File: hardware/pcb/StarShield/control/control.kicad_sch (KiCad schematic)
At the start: 9 parts, among them J3A nice!nano v2 左列 (PM 1-12), J3B nice!nano v2 右列 (PM 13-24), SW1 PCM13 (SP3T), U2 74HC595, U3 74HC595, U4 74HC595

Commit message: feat(schematic): M5 RGB 子图 —— 95 颗 SK6812MINI-E 数据链，原理图四张子图齐
新增第 6 张子图 rgb/rgb.kicad_sch（A2；95 灯珠 / 380 条引脚连接）：
- 数据源 rgb_design.py 由 docs/_generated/matrix.json 循环生成（位号 LED1..95 ↔ 键 index），
  链序 = 键位 index 顺序（行优先、行内从左到右），与 ZMK 侧 LED index 一致。
- LED1.DIN ← 全局 LED_DIN（控制子图 J3A.1 = P0.06 / spi3 MOSI）；LED95.DOUT 链尾 NC。
- 供电：全部 VDD → 全局 VLED（电源子图 Q1 门控的电池直供轨）；VSS → GND。
- 符号用官方 LED:SK6812MINI-E（派生符号已展平）；封装选 PLCC4 3.5x3.5 正装，
  型号-封装对应与贴装方向标 UNVERIFIED（B3/B4 用实物核对）。
- 根图改 3 列 x 2 行布局以容纳 6 张子图。
- verify_rgb.py：派生 / 跨图接口 / 具名（链序、链尾、供电）/ ERC 四组断言。

ERC：根图整体 0 error，isolated 两条（VLED / LED_DIN）就此归零。
同步：控制子图与 RGB 子图移除重复的 GND PWR_FLAG（全局网只能有一个 power output，
否则触发 ERC pin_to_pin error），改由电源子图统一提供；verify_control 断言同步。
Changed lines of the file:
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@@
-		(pin "1")
-	)
-	(symbol (lib_id "power:PWR_FLAG") (at 33.02 171.45 0) (unit 1)
-		(exclude_from_sim no) (in_bom yes) (on_board yes) (dnp no) (fields_autoplaced yes)
-	(property "Reference" "#FLG01" (at 33.02 166.37 0)
-			(effects (font (size 1.27 1.27)) (hide yes)))
-	(property "Value" "PWR_FLAG" (at 33.02 176.53 0)
-			(effects (font (size 1.27 1.27)) (hide yes)))
-	(property "Footprint" "" (at 33.02 171.45 0)
-			(effects (font (size 1.27 1.27)) (hide yes)))
-	(property "Datasheet" "" (at 33.02 171.45 0)
-			(effects (font (size 1.27 1.27)) (hide yes)))
-		(pin "1")
-	)
-	(symbol (lib_id "power:GND") (at 33.02 171.45 0) (unit 1)
-		(exclude_from_sim no) (in_bom yes) (on_board yes) (dnp no) (fields_autoplaced yes)
-	(property "Reference" "#PWR02175" (at 33.02 166.37 0)
-			(effects (font (size 1.27 1.27)) (hide yes)))
-	(property "Value" "GND" (at 33.02 176.53 0)
-			(effects (font (size 1.27 1.27)) (hide yes)))
-	(property "Footprint" "" (at 33.02 171.45 0)
-			(effects (font (size 1.27 1.27)) (hide yes)))
-	(property "Datasheet" "" (at 33.02 171.45 0)
-			(effects (font (size 1.27 1.27)) (hide yes)))
 		(pin "1")
 	)

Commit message: feat(b3): 新增封装存在性核查 + 排针封装定案
- 新增 docs/_tools/verify_footprints.py：扫描 4 张子图的 Footprint 属性，
  逐个去 KiCad 封装库查存在性 —— 「封装存不存在」从此是可复现断言，
  不再靠人工看（95 个热插拔座封装缺失就是这样默默存在的）。
- 实测：218 / 313 个元件的封装在官方库（13 种）。
- J3A/J3B 定案 Connector_PinSocket_2.54mm:PinSocket_1x12_P2.54mm_Vertical
  （官方库无 Connector_Mill-Max；排母孔径 1.0 vs Mill-Max 推荐 0.94mm 可焊，
  料号与孔径并入 B6 实物核对）。
- 唯一未决：MX 热插拔座封装（95 个）—— 官方库没有；社区库 CC BY-SA 4.0
  无官方库的「用于设计不受约束」例外，抄了会污染 CERN-OHL-S 链 ⇒ 不可引入。
  出路为「自画」或「改轴体直焊（官方封装现成且键宽全覆盖）」，待用户拍板。
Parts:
- J3A, J3B: footprint ❓待定（Mill-Max 插座，B3/B4 定） -> Connector_PinSocket_2.54mm:PinSocket_1x12_P2.54mm_Vertical; MPN (none) -> Mill-Max 315-43-112-41-001000 ❓待核
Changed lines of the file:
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@@
 	(property "Value" "nice!nano v2 左列 (PM 1-12)" (at 50.8 144.78 0)
 			(effects (font (size 1.27 1.27))))
-	(property "Footprint" "❓待定（Mill-Max 插座，B3/B4 定）" (at 50.8 139.7 0)
+	(property "Footprint" "Connector_PinSocket_2.54mm:PinSocket_1x12_P2.54mm_Vertical" (at 50.8 139.7 0)
 			(effects (font (size 1.27 1.27)) (hide yes)))
 	(property "Datasheet" "" (at 50.8 139.7 0)
+			(effects (font (size 1.27 1.27)) (hide yes)))
+		(property "MPN" "Mill-Max 315-43-112-41-001000 ❓待核" (at 50.8 139.7 0)
 			(effects (font (size 1.27 1.27)) (hide yes)))
 		(property "Note" "J3A.n = Pro Micro 标号 n；映射依据 ZMK arduino_pro_micro_pins.dtsi" (at 50.8 139.7 0)
@@
 	(property "Value" "nice!nano v2 右列 (PM 13-24)" (at 76.2 144.78 0)
 			(effects (font (size 1.27 1.27))))
-	(property "Footprint" "❓待定（Mill-Max 插座，B3/B4 定）" (at 76.2 139.7 0)
+	(property "Footprint" "Connector_PinSocket_2.54mm:PinSocket_1x12_P2.54mm_Vertical" (at 76.2 139.7 0)
 			(effects (font (size 1.27 1.27)) (hide yes)))
 	(property "Datasheet" "" (at 76.2 139.7 0)
 			(effects (font (size 1.27 1.27)) (hide yes)))
+		(property "MPN" "Mill-Max 315-43-112-41-001000 ❓待核" (at 76.2 139.7 0)
+			(effects (font (size 1.27 1.27)) (hide yes)))
 		(property "Note" "J3B.n = Pro Micro 标号 12+n；RAW(PM13) 接 OUT，VCC(PM16) 是 3.3V 轨" (at 76.2 139.7 0)

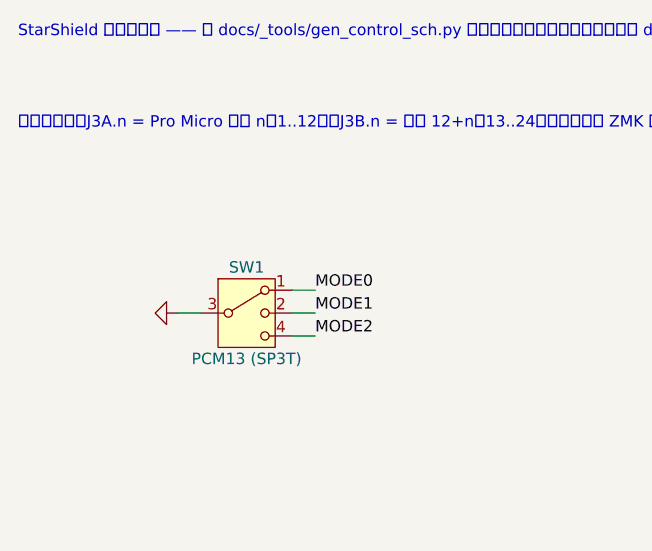
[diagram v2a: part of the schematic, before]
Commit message: fix(hw): 三档开关位号 SW1 -> SW96（与矩阵第一个开关重名）
根图整体网表里两个元件的引脚会并到同一个位号下；PCB 上会出现两个 SW1。
现有校验假通过：verify_netlist 数的是 SW 前缀的不同名字个数，
95 个矩阵开关 + 1 个 SP3T 因重名去重后仍是 95 个。

- control_design.py: ref 与 4 条连接改名 SW96（顺延 D96 的编号习惯）
- verify_control.py: 4 条开关断言改按 SW96
- verify_netlist.py: 矩阵开关显式只数 SW1..SW95（不再用前缀计数）
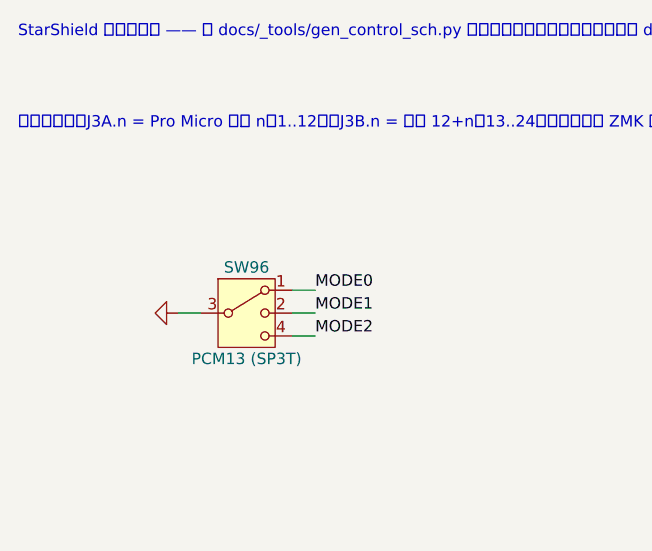
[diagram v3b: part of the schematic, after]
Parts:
- removed SW1: PCM13 (SP3T), Button_Switch_SMD:SW_SP3T_PCM13, symbol Switch:SW_SP3T
- added SW96: PCM13 (SP3T), Button_Switch_SMD:SW_SP3T_PCM13, symbol Switch:SW_SP3T
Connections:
- net GND: now also SW96.3
- net MODE0: now also SW96.1
- net MODE1: now also SW96.2
- net MODE2: now also SW96.4
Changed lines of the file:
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@@
 	(symbol (lib_id "Switch:SW_SP3T") (at 50.8 63.5 0) (unit 1)
 		(exclude_from_sim no) (in_bom yes) (on_board yes) (dnp no) (fields_autoplaced yes)
-	(property "Reference" "SW1" (at 50.8 58.42 0)
+	(property "Reference" "SW96" (at 50.8 58.42 0)
 			(effects (font (size 1.27 1.27))))
 	(property "Value" "PCM13 (SP3T)" (at 50.8 68.58 0)

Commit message: fix(b6-1): J3A/J3B 由 1x12 改 1x13（按 nice!nano v2 实物孔序），走线零改动
背景：2026-09-19 实物核对发现 nice!nano v2 每排 13 孔（官方 pinout 图 + 实物清点），
原 1x12 设计会把 J3B 的 VCC 插到实物 RESET 上、J3A 整排错位一孔。

关键洞察：官方孔序去掉第 1 孔后与旧 12 孔的网**逐孔一致** ⇒
只需在 USB 端左侧（x=37.46）加一个孔（J3A 加 GND、J3B 加 OUT）+ Pad 号整体后移一位，
**走线一根都不用动**。（反面做法「网络整体后移一孔」实测撞出 8 处 shorting_items +
2 处 tracks_crossing，已否决。）

改动：
- extract_power_symbols.py：符号缓存加 Connector_Generic:Conn_01x13（取代 01x12）
- control_design.py：J3A/J3B 改 Conn_01x13、CONN 表按官方孔序重排、页脚注更新
- control.kicad_sch / rgb.kicad_sch：生成链重跑产物
- verify_control.py / verify_rgb.py：断言孔号同步（LED_DIN 由 J3A.1 改 J3A.2）
- rgb_design.py：注释里的 J3A.1 改 J3A 孔2
- Starshield.kicad_pcb：J3A/J3B 各加第 13 孔、Pad 号重排、J3B 孔1-孔2 OUT 同网桥、
  重填铺铜（未连通 0、未豁免 error 0）
- docs/nice-nano-physical-verification.md：§4 落点修正（座口 x≈32.2）、§6 量测结论与执行记录

校验：七项校验器全绿；生成链确定性复核通过（重跑生成器后 git status 无变化）。
固件 overlay 零改动（D 编号 ↔ GPIO 映射不变）。
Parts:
- J3A: value nice!nano v2 左列 (PM 1-12) -> nice!nano v2 左列 (孔 1-13); footprint Connector_PinSocket_2.54mm:PinSocket_1x12_P2.54mm_Vertical -> Connector_PinSocket_2.54mm:PinSocket_1x13_P2.54mm_Vertical; symbol Connector_Generic:Conn_01x12 -> Connector_Generic:Conn_01x13; MPN Mill-Max 315-43-112-41-001000 ❓待核 -> Mill-Max 315-43-113-41-001000 ❓待核; Note J3A.n = Pro Micro 标号 n；映射依据 ZMK arduino_pro_micro_pins.dtsi -> J3A.n = 实物孔位序号（USB 端起）；D 编号见注释，依据 ZMK gpio-map
- J3B: value nice!nano v2 右列 (PM 13-24) -> nice!nano v2 右列 (孔 1-13); footprint Connector_PinSocket_2.54mm:PinSocket_1x12_P2.54mm_Vertical -> Connector_PinSocket_2.54mm:PinSocket_1x13_P2.54mm_Vertical; symbol Connector_Generic:Conn_01x12 -> Connector_Generic:Conn_01x13; MPN Mill-Max 315-43-112-41-001000 ❓待核 -> Mill-Max 315-43-113-41-001000 ❓待核; Note J3B.n = Pro Micro 标号 12+n；RAW(PM13) 接 OUT，VCC(PM16) 是 3.3V 轨 -> J3B.1/2 = B+(RAW) 接 OUT；孔 5 = 3.3V(VCC)；孔 4 = RESET 不接
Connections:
- net 595_MOSI: now also J3B.12 (Pin_12); no longer J3B.11 (Pin_11)
- net 595_RCLK: now also J3B.8 (Pin_8); no longer J3B.7 (Pin_7)
- net 595_SCK: now also J3B.10 (Pin_10); no longer J3B.9 (Pin_9)
- net GND: now also J3A.1 (Pin_1), J3A.5 (Pin_5), J3B.3 (Pin_3); no longer J3A.3 (Pin_3), J3B.2 (Pin_2)
- net LED_DIN: now also J3A.2 (Pin_2); no longer J3A.1 (Pin_1)
- net MODE0: now also J3A.6 (Pin_6); no longer J3A.5 (Pin_5)
- net MODE1: now also J3B.11 (Pin_11); no longer J3B.10 (Pin_10)
- net MODE2: now also J3B.9 (Pin_9); no longer J3B.8 (Pin_8)
- net OUT: now also J3B.2 (Pin_2)
- net RGB_PWR_EN: now also J3B.13 (Pin_13); no longer J3B.12 (Pin_12)
- net ROW0: now also J3A.8 (Pin_8); no longer J3A.7 (Pin_7)
- net ROW1: now also J3A.9 (Pin_9); no longer J3A.8 (Pin_8)
- net ROW2: now also J3A.10 (Pin_10); no longer J3A.9 (Pin_9)
- net ROW3: now also J3A.11 (Pin_11); no longer J3A.10 (Pin_10)
- net ROW4: now also J3A.13 (Pin_13); no longer J3A.12 (Pin_12)
- net ROW5: now also J3A.12 (Pin_12); no longer J3A.11 (Pin_11)
- net VCC: now also J3B.5 (Pin_5); no longer J3B.4 (Pin_4)
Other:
- note added: "【供电】J3B.1/2(B+) 接电源子图 OUT（系统轨 3.0-4.4V，电池/USB 较高者）—— nice!nano 板载稳压后输出 VCC(孔 5) 3.3V，给 3 颗 595 供电（负载轻，远低于 VCC 能力）。WS2812 供电走 VLED（电源子图 Q1 门控后的 LED 轨），不在本子图 —— 见 RGB 子图(M5)"
- note added: "【投板前核对】1) nice!nano 排针 pitch/脚数已由 B6 实物核对（每排 13 孔，已改 1x13）2) PCM13 封装 pad 与符号掷点对应（B3/B4）3) J3A.12/13 = ROW5/ROW4 的交错顺序与 overlay row-gpios 一一对应（已按 overlay 核实，但 PCB 布局时仍需复核）4) 排针针径与母座孔径、第五项：USB 口伸出量决定外壳开孔"
- note added: "【排针映射】J3A.n / J3B.n = nice!nano v2 **实物孔位序号（自 USB 端起，每排 13 孔）**。2026-09-19 B6 实物核对 + 官方 pinout 图确认每排 13 孔（比 Pro Micro 多 1 孔，多在 USB 端）；原 1x12 映射已作废。D 编号 ↔ GPIO 仍依 ZMK arduino_pro_micro_pins.dtsi，与孔位序号无关。逐孔映射表见 docs/nice-nano-physical-verification.md §6.2"
- note removed: "【供电】J3B.13(RAW) 接电源子图 OUT（系统轨 3.0-4.4V，电池/USB 较高者）—— nice!nano 板载稳压后输出 VCC(PM16) 3.3V，给 3 颗 595 供电（负载轻，远低于 VCC 能力）。WS2812 供电走 VLED（电源子图 Q1 门控后的 LED 轨），不在本子图 —— 见 RGB 子图(M5)"
- note removed: "【投板前核对】1) nice!nano 排针 pitch/脚数（B6）2) PCM13 封装 pad 与符号掷点对应（B3/B4）3) J3A.11/12 = ROW5/ROW4 的交错顺序与 overlay row-gpios 一一对应（已按 overlay 核实，但 PCB 布局时仍需复核）"
- note removed: "【排针映射】J3A.n = Pro Micro 标号 n（1..12），J3B.n = 标号 12+n（13..24）。映射来自 ZMK 官方 v0.3 nice_nano 的 arduino_pro_micro_pins.dtsi。投板前必须用实物核对排针 pitch / 每边脚数（handoff B6）"

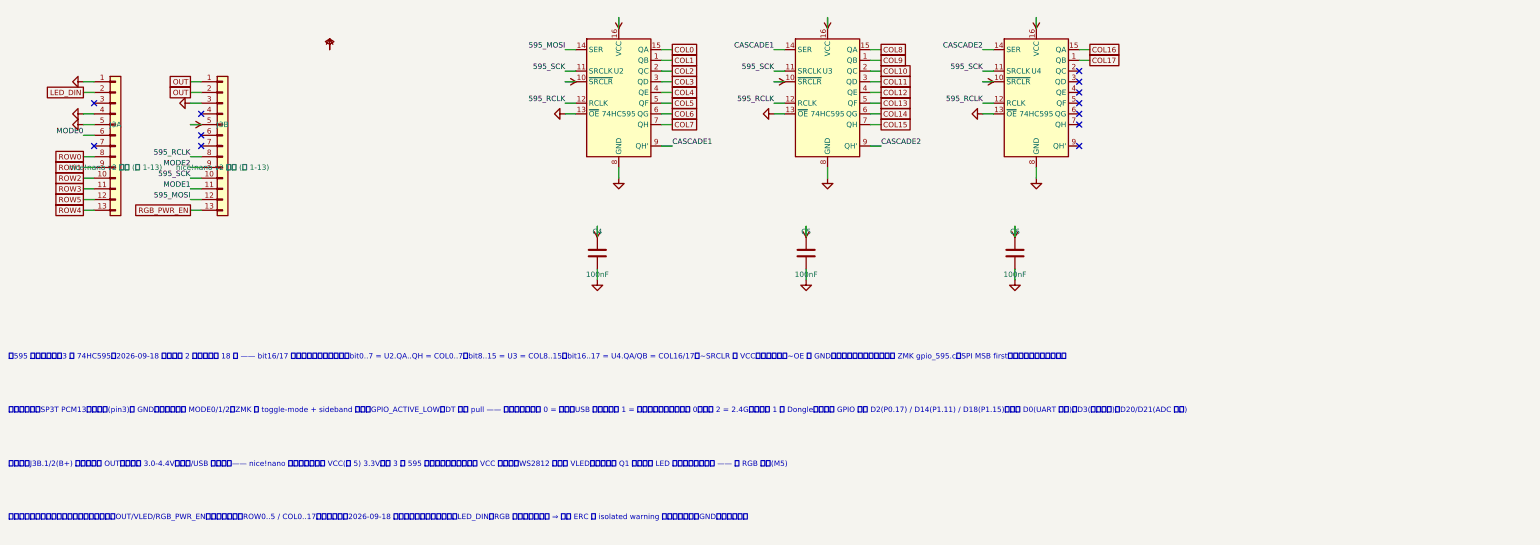
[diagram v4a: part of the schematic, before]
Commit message: feat(power): 方案①落地 —— 模块 B+/RAW 由 OUT 改接 VBAT（插模块口即充电）；模块整组左移 + J1 让位
背景（用户质疑成立）：商业键盘一律「一个口 = 数据 + 充电」（Kisnt KN85 / 雷柏 V700-8A /
CHERRY KW 9200 官方口径）；社区 nice!nano 方案把电池挂在模块自带充电器输出上，插模块口即充电。
我们原先把电池接自研 BQ24072 的 BAT、模块挂 OUT ⇒ 模块充电器的电流进不了电池
（OUT→BAT 不是充电路径）⇒ 有线模式下充不上电。

改动：
- 电路：J3B 孔1/孔2（B+/RAW）网络 OUT -> VBAT；VBAT 由电源子图局部网升为跨子图全局网
  （power_design.py 与 control_design.py 的 GLOBAL_NETS 各加 VBAT）
- 子图：power.kicad_sch / control.kicad_sch 重生成（版式自检通过）
- 校验：verify_control 断言改为「VBAT 跨图连通（J3B 孔1/2 + U1/J2/C3）」+
  「OUT 不再挂 J3B」；网表类五项校验全绿
- 几何（B6-2）：nice!nano 插座整组左移 30.46 mm（孔1 x=7.00、口面 x=1.70 与壳面齐平）；
  J1/R1/R2/F1 让位到 x=155-168；pcb_design.py 同步
- 板文件：J3B 孔1/2 改网为 VBAT（旧 OUT 走线已随左移一并清除）
- 文档：power-architecture.md §1 / bq24072-pinout.md §2.3 / decisions.md 电源段各加「重载仍接 OUT、
  模块为唯一例外」的修订说明；量测文档 §6.6 记录完整对标与代价

⚠️ 遗留（下一步）：肩部走线缺口待补（左移时删了 76 项），Freerouting 正在用新网表全板重布；
完成后需重跑 DRC + 七项校验器。
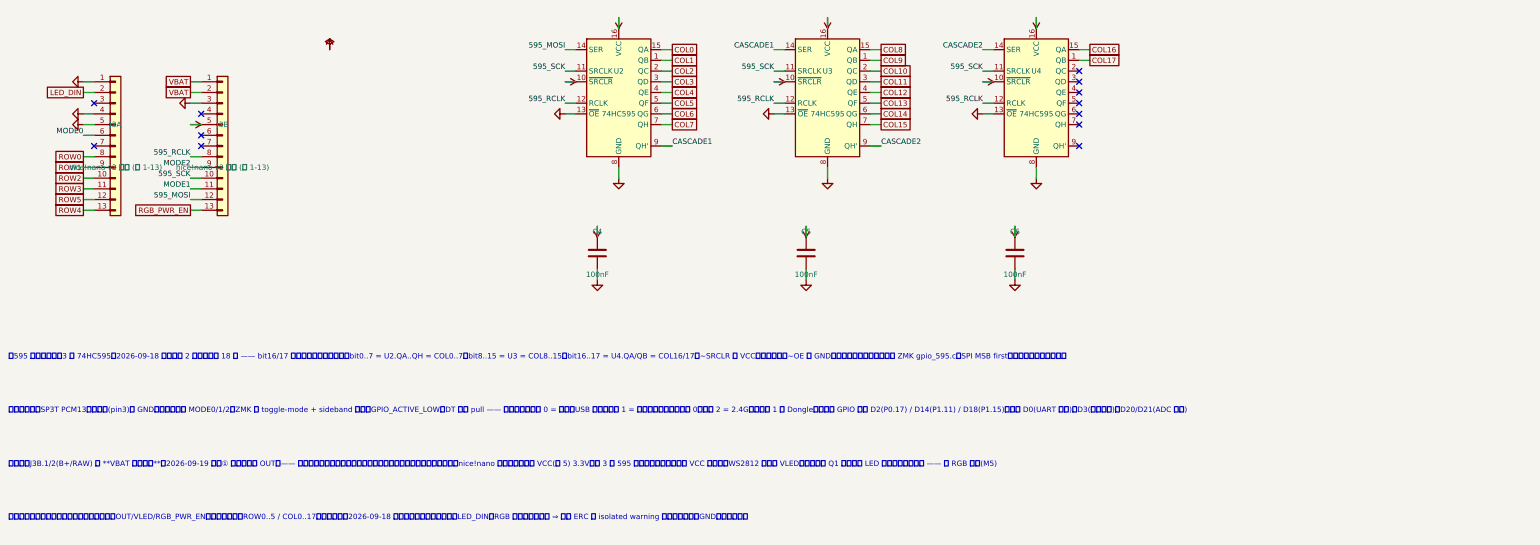
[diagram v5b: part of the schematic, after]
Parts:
- J3B: Note J3B.1/2 = B+(RAW) 接 OUT；孔 5 = 3.3V(VCC)；孔 4 = RESET 不接 -> J3B.1/2 = B+/RAW 接 VBAT 电池节点（2026-09-19 方案①）；孔 5 = 3.3V(VCC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
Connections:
- net OUT renamed VBAT
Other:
- note added: "【供电】J3B.1/2(B+/RAW) 接 **VBAT 电池节点**（2026-09-19 方案① 改接，原为 OUT）—— 如此插模块口即由模块自带充电器给电池充电（有线模式也充电）。nice!nano 板载稳压后输出 VCC(孔 5) 3.3V，给 3 颗 595 供电（负载轻，远低于 VCC 能力）。WS2812 供电走 VLED（电源子图 Q1 门控后的 LED 轨），不在本子图 —— 见 RGB 子图(M5)"
- note removed: "【供电】J3B.1/2(B+) 接电源子图 OUT（系统轨 3.0-4.4V，电池/USB 较高者）—— nice!nano 板载稳压后输出 VCC(孔 5) 3.3V，给 3 颗 595 供电（负载轻，远低于 VCC 能力）。WS2812 供电走 VLED（电源子图 Q1 门控后的 LED 轨），不在本子图 —— 见 RGB 子图(M5)"
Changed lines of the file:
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@@
 	(wire (pts (xy 71.12 124.46) (xy 68.58 124.46))
 		(stroke (width 0) (type default)))
-	(global_label "OUT" (shape passive) (at 68.58 124.46 180) (fields_autoplaced yes)
+	(global_label "VBAT" (shape passive) (at 68.58 124.46 180) (fields_autoplaced yes)
 		(effects (font (size 1.27 1.27)) (justify right))
 	)
 	(wire (pts (xy 71.12 127.0) (xy 68.58 127.0))
 		(stroke (width 0) (type default)))
-	(global_label "OUT" (shape passive) (at 68.58 127.0 180) (fields_autoplaced yes)
+	(global_label "VBAT" (shape passive) (at 68.58 127.0 180) (fields_autoplaced yes)
 		(effects (font (size 1.27 1.27)) (justify right))
 	)
@@
 		(property "MPN" "Mill-Max 315-43-113-41-001000 ❓待核" (at 76.2 139.7 0)
 			(effects (font (size 1.27 1.27)) (hide yes)))
-		(property "Note" "J3B.1/2 = B+(RAW) 接 OUT；孔 5 = 3.3V(VCC)；孔 4 = RESET 不接" (at 76.2 139.7 0)
+		(property "Note" "J3B.1/2 = B+/RAW 接 VBAT 电池节点（2026-09-19 方案①）；孔 5 = 3.3V(VCC)；孔 4 = RESET 不接" (at 76.2 139.7 0)
 			(effects (font (size 1.27 1.27)) (hide yes)))
 		(pin "1")
@@
 		(effects (font (size 1.27 1.27)) (justify left bottom))
 )
-	(text "【供电】J3B.1/2(B+) 接电源子图 OUT（系统轨 3.0-4.4V，电池/USB 较高者）—— nice!nano 板载稳压后输出 VCC(孔 5) 3.3V，给 3 颗 595 供电（负载轻，远低于 VCC 能力）。WS2812 供电走 VLED（电源子图 Q1 门控后的 LED 轨），不在本子图 —— 见 RGB 子图(M5)" (exclude_from_sim no) (at 25.4 216.0 0)
+	(text "【供电】J3B.1/2(B+/RAW) 接 **VBAT 电池节点**（2026-09-19 方案① 改接，原为 OUT）—— 如此插模块口即由模块自带充电器给电池充电（有线模式也充电）。nice!nano 板载稳压后输出 VCC(孔 5) 3.3V，给 3 颗 595 供电（负载轻，远低于 VCC 能力）。WS2812 供电走 VLED（电源子图 Q1 门控后的 LED 轨），不在本子图 —— 见 RGB 子图(M5)" (exclude_from_sim no) (at 25.4 216.0 0)
 		(effects (font (size 1.27 1.27)) (justify left bottom))
 )
